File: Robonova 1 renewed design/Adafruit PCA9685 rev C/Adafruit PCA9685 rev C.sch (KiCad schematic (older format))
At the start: 28 parts, among them J1 TERMBLOCK_1X2, Q1 AOD417, U1 PCA9685

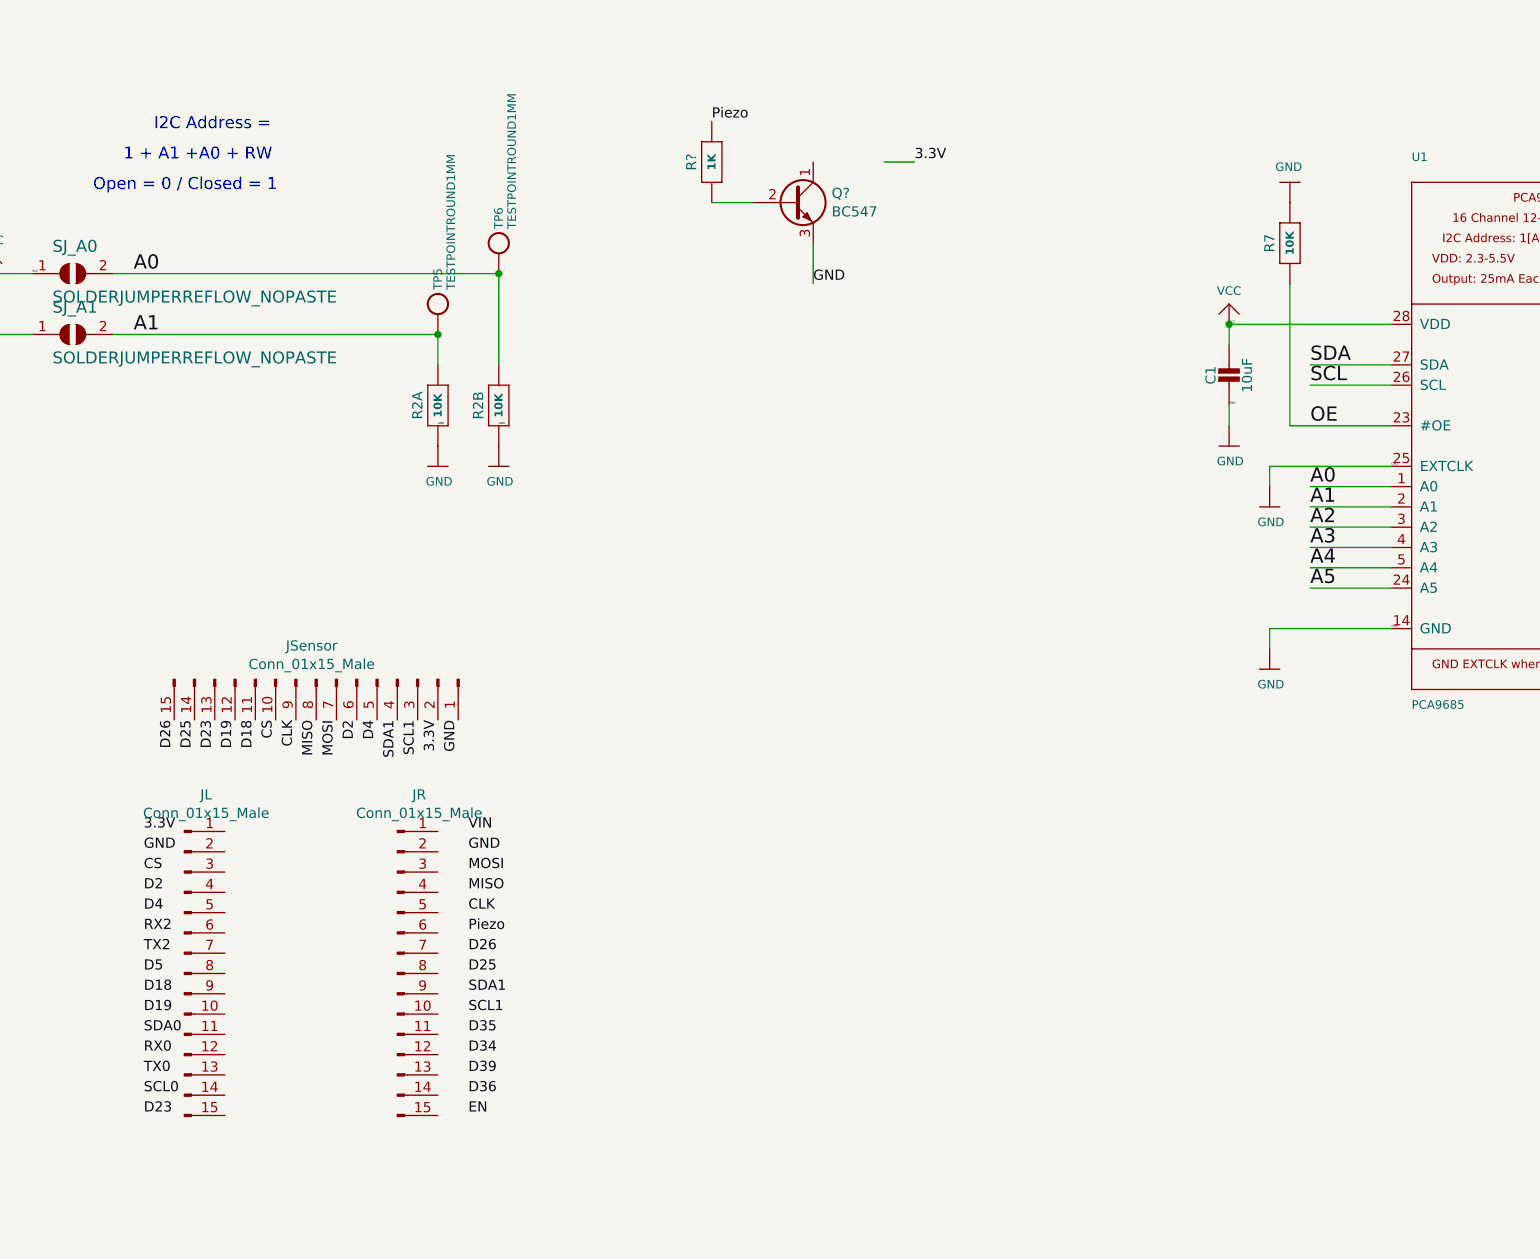
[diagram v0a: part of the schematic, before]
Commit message: Global pcb layout sketch and obtained data
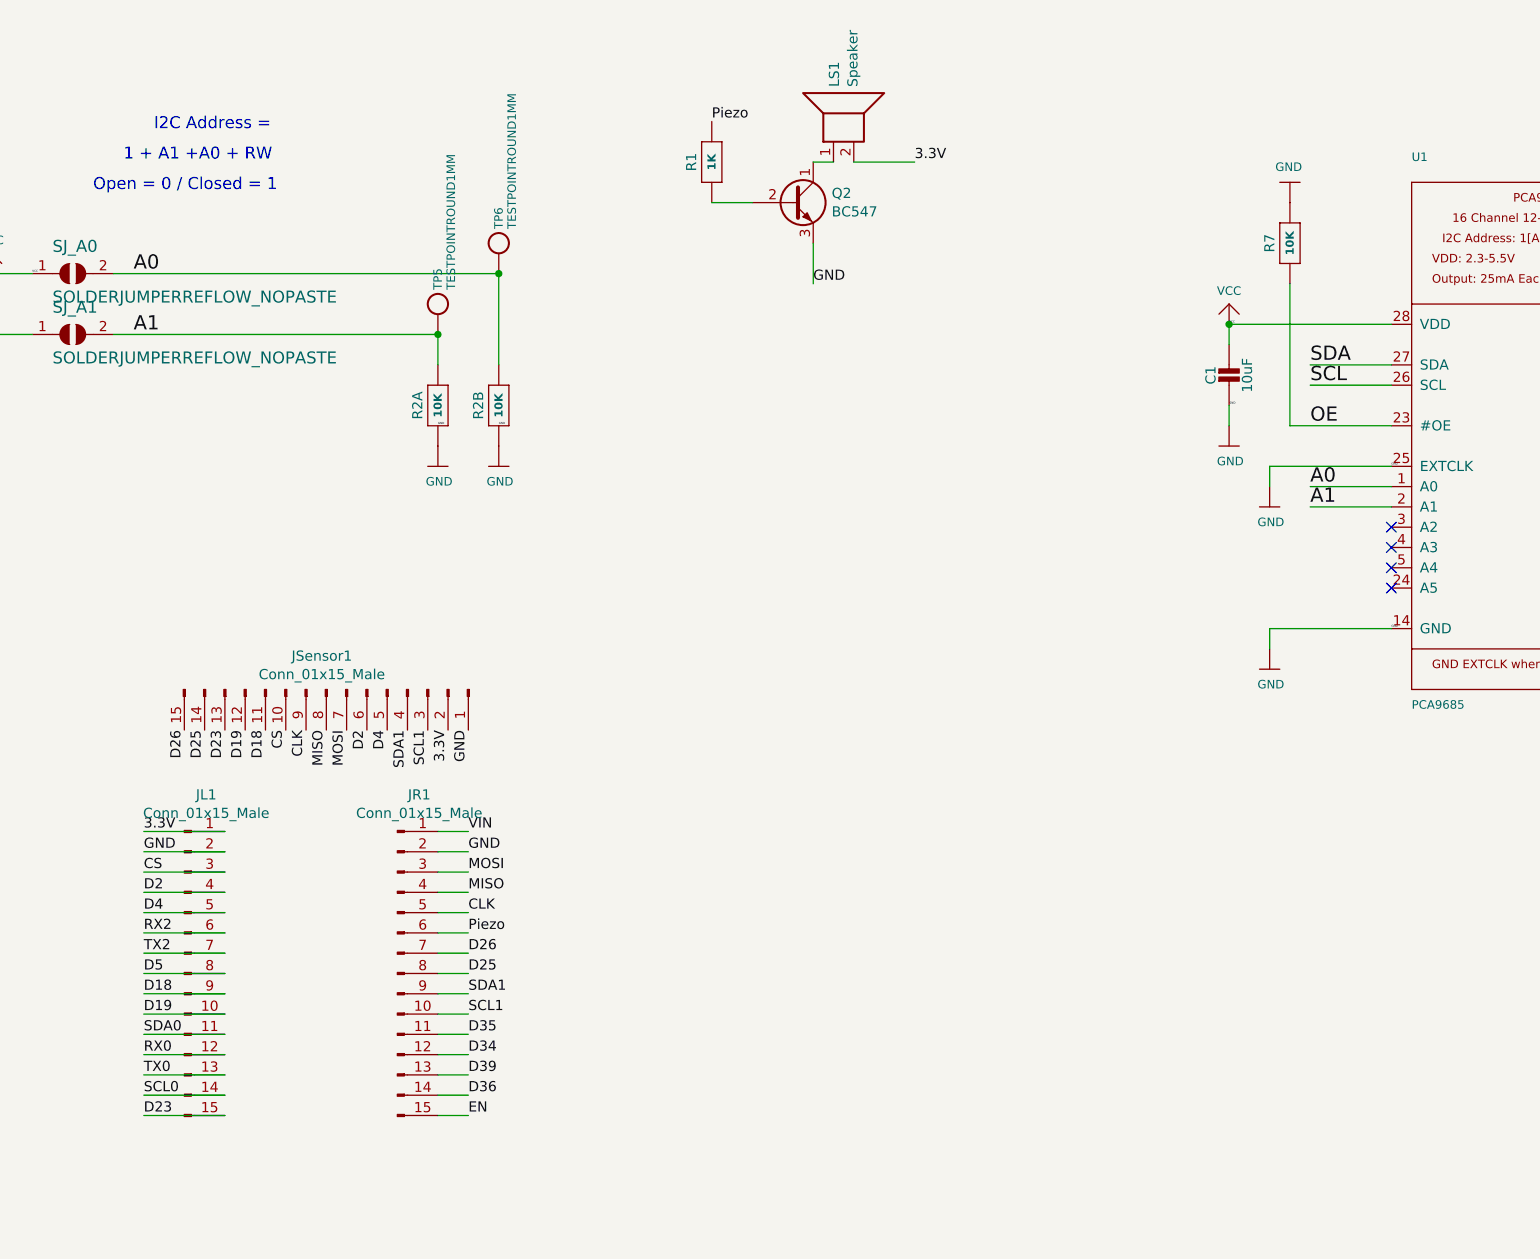
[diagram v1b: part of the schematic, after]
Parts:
- added LS1: Speaker, Capacitor_THT:CP_Radial_D12.5mm_P7.50mm, symbol Device:Speaker
- JL1: renamed from JL; footprint (none) -> Connector_PinHeader_2.54mm:PinHeader_1x15_P2.54mm_Vertical
- JR1: renamed from JR; footprint (none) -> Connector_PinHeader_2.54mm:PinHeader_1x15_P2.54mm_Vertical
- JSensor1: renamed from JSensor; footprint (none) -> Connector_PinHeader_2.54mm:PinHeader_1x15_P2.54mm_Vertical
- gave numbers to parts that had none: 2
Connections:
- net labels removed: A2, A3, A4, A5
- wire segments 138 -> 165
- no-connect marks 0 -> 4
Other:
- moved on the sheet: JSensor1
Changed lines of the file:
@@
 A1
-Wire Wire Line
-	7100 2250 6700 2250
-Text Label 6700 2250 0    70   ~ 0
-A2
-Wire Wire Line
-	7100 2350 6700 2350
-Text Label 6700 2350 0    70   ~ 0
-A3
-Wire Wire Line
-	7100 2450 6700 2450
-Text Label 6700 2450 0    70   ~ 0
-A4
-Wire Wire Line
-	7100 2550 6700 2550
-Text Label 6700 2550 0    70   ~ 0
-A5
 Wire Wire Line
 	6300 1250 6300 1350
@@
 F 3 "" H 600 1000 50  0001 C CNN
 	1    600  1000
-	1    0    0    -1
-$EndComp
-$Comp
-L Connector:Conn_01x15_Male JR
-U 1 1 623963E7
-P 2200 4450
-F 0 "JR" H 2308 5331 50  0000 C CNN
-F 1 "Conn_01x15_Male" H 2308 5240 50  0000 C CNN
-F 2 "" H 2200 4450 50  0001 C CNN
-F 3 "~" H 2200 4450 50  0001 C CNN
-	1    2200 4450
-	1    0    0    -1
-$EndComp
-$Comp
-L Connector:Conn_01x15_Male JL
-U 1 1 623A1462
-P 1150 4450
-F 0 "JL" H 1258 5331 50  0000 C CNN
-F 1 "Conn_01x15_Male" H 1258 5240 50  0000 C CNN
-F 2 "" H 1150 4450 50  0001 C CNN
-F 3 "~" H 1150 4450 50  0001 C CNN
-	1    1150 4450
 	1    0    0    -1
 $EndComp
@@
 Text Label 2550 5150 0    50   ~ 0
 EN
-$Comp
-L Connector:Conn_01x15_Male JSensor
-U 1 1 623D16C9
-P 1800 3000
-F 0 "JSensor" V 1635 2978 50  0000 C CNN
-F 1 "Conn_01x15_Male" V 1726 2978 50  0000 C CNN
-F 2 "" H 1800 3000 50  0001 C CNN
-F 3 "~" H 1800 3000 50  0001 C CNN
-	1    1800 3000
-	0    1    1    0
-$EndComp
-Text Label 1100 3200 3    50   ~ 0
+Text Label 1150 3250 3    50   ~ 0
 D26
-Text Label 1200 3200 3    50   ~ 0
+Text Label 1250 3250 3    50   ~ 0
 D25
-Text Label 1300 3200 3    50   ~ 0
+Text Label 1350 3250 3    50   ~ 0
 D23
-Text Label 1400 3200 3    50   ~ 0
+Text Label 1450 3250 3    50   ~ 0
 D19
-Text Label 1500 3200 3    50   ~ 0
+Text Label 1550 3250 3    50   ~ 0
 D18
-Text Label 1600 3200 3    50   ~ 0
+Text Label 1650 3250 3    50   ~ 0
 CS
-Text Label 1700 3200 3    50   ~ 0
+Text Label 1750 3250 3    50   ~ 0
 CLK
-Text Label 1800 3200 3    50   ~ 0
+Text Label 1850 3250 3    50   ~ 0
 MISO
-Text Label 1900 3200 3    50   ~ 0
+Text Label 1950 3250 3    50   ~ 0
 MOSI
-Text Label 2000 3200 3    50   ~ 0
+Text Label 2050 3250 3    50   ~ 0
 D2
-Text Label 2100 3200 3    50   ~ 0
+Text Label 2150 3250 3    50   ~ 0
 D4
-Text Label 2200 3200 3    50   ~ 0
+Text Label 2250 3250 3    50   ~ 0
 SDA1
-Text Label 2300 3200 3    50   ~ 0
+Text Label 2350 3250 3    50   ~ 0
 SCL1
-Text Label 2400 3200 3    50   ~ 0
+Text Label 2450 3250 3    50   ~ 0
 3.3V
-Text Label 2500 3200 3    50   ~ 0
+Text Label 2550 3250 3    50   ~ 0
 GND
 $Comp
-L Transistor_BJT:BC547 Q?
+L Transistor_BJT:BC547 Q2
 U 1 1 6249BC27
 P 4150 650
-F 0 "Q?" H 4341 696 50  0000 L CNN
+F 0 "Q2" H 4341 696 50  0000 L CNN
 F 1 "BC547" H 4341 605 50  0000 L CNN
 F 2 "Package_TO_SOT_THT:TO-92_Inline" H 4350 575 50  0001 L CIN
@@
 $EndComp
 $Comp
-L Adafruit-PCA9685-rev-C-rescue:RESISTOR0805_NOOUTLINE-Adafruit_PCA9685_rev_C-eagle-import R?
+L Adafruit-PCA9685-rev-C-rescue:RESISTOR0805_NOOUTLINE-Adafruit_PCA9685_rev_C-eagle-import R1
 U 1 1 624A02EE
 P 3750 450
-F 0 "R?" H 3750 550 50  0000 C CNN
+F 0 "R1" H 3750 550 50  0000 C CNN
 F 1 "1K" H 3750 450 40  0000 C CNB
 F 2 "Adafruit PCA9685 rev C:0805-NO" H 3750 450 50  0001 C CNN
@@
 	4250 850  4250 1050
 Wire Wire Line
-	4600 450  4750 450
-Wire Wire Line
 	3750 650  3950 650
+$Comp
+L Device:Speaker LS1
+U 1 1 62515CA3
+P 4350 250
+F 0 "LS1" H 4520 246 50  0000 L CNN
+F 1 "Speaker" H 4520 155 50  0000 L CNN
+F 2 "Capacitor_THT:CP_Radial_D12.5mm_P7.50mm" H 4350 50  50  0001 C CNN
+F 3 "~" H 4340 200 50  0001 C CNN
+	1    4350 250
+	0    -1   -1   0
+$EndComp
+Wire Wire Line
+	4450 450  4750 450
+Wire Wire Line
+	4350 450  4250 450
+NoConn ~ 7100 2350
+NoConn ~ 7100 2450
+NoConn ~ 7100 2550
+NoConn ~ 7100 2250
+Wire Wire Line
+	2400 3750 2550 3750
+Wire Wire Line
+	2400 3850 2550 3850
+Wire Wire Line
+	2400 3950 2550 3950
+Wire Wire Line
+	2400 4050 2550 4050
+Wire Wire Line
+	2400 4150 2550 4150
+Wire Wire Line
+	2400 4250 2550 4250
+Wire Wire Line
+	2400 4350 2550 4350
+Wire Wire Line
+	2400 4450 2550 4450
+Wire Wire Line
+	2400 4550 2550 4550
+Wire Wire Line
+	2400 4650 2550 4650
+Wire Wire Line
+	2400 4750 2550 4750
+Wire Wire Line
+	2400 4850 2550 4850
+Wire Wire Line
+	2400 4950 2550 4950
+Wire Wire Line
+	2400 5050 2550 5050
+Wire Wire Line
+	2400 5150 2550 5150
+Wire Wire Line
+	950  3750 1350 3750
+Wire Wire Line
+	950  3850 1350 3850
+Wire Wire Line
+	950  3950 1350 3950
+Wire Wire Line
+	950  4050 1350 4050
+Wire Wire Line
+	950  4150 1350 4150
+Wire Wire Line
+	950  4250 1350 4250
+Wire Wire Line
+	950  4350 1350 4350
+Wire Wire Line
+	950  4450 1350 4450
+Wire Wire Line
+	950  4550 1350 4550
+Wire Wire Line
+	950  4650 1350 4650
+Wire Wire Line
+	950  4750 1350 4750
+Wire Wire Line
+	950  4850 1350 4850
+Wire Wire Line
+	950  4950 1350 4950
+Wire Wire Line
+	950  5050 1350 5050
+Wire Wire Line
+	950  5150 1350 5150
+$Comp
+L Connector:Conn_01x15_Male JSensor1
+U 1 1 623D16C9
+P 1850 3050
+F 0 "JSensor1" V 1685 3028 50  0000 C CNN
+F 1 "Conn_01x15_Male" V 1776 3028 50  0000 C CNN
+F 2 "Connector_PinHeader_2.54mm:PinHeader_1x15_P2.54mm_Vertical" H 1850 3050 50  0001 C CNN
+F 3 "~" H 1850 3050 50  0001 C CNN
+	1    1850 3050
+	0    1    1    0
+$EndComp
+$Comp
+L Connector:Conn_01x15_Male JR1
+U 1 1 623963E7
+P 2200 4450
+F 0 "JR1" H 2308 5331 50  0000 C CNN
+F 1 "Conn_01x15_Male" H 2308 5240 50  0000 C CNN
+F 2 "Connector_PinHeader_2.54mm:PinHeader_1x15_P2.54mm_Vertical" H 2200 4450 50  0001 C CNN
+F 3 "~" H 2200 4450 50  0001 C CNN
+	1    2200 4450
+	1    0    0    -1
+$EndComp
+$Comp
+L Connector:Conn_01x15_Male JL1
+U 1 1 623A1462
+P 1150 4450
+F 0 "JL1" H 1258 5331 50  0000 C CNN
+F 1 "Conn_01x15_Male" H 1258 5240 50  0000 C CNN
+F 2 "Connector_PinHeader_2.54mm:PinHeader_1x15_P2.54mm_Vertical" H 1150 4450 50  0001 C CNN
+F 3 "~" H 1150 4450 50  0001 C CNN
+	1    1150 4450
+	1    0    0    -1
+$EndComp
 $EndSCHEMATC
